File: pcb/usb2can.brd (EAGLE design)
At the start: 57.8 x 17.2 mm, 35 parts, among them CON1 USB_A_MALESMD, IC1 ADM3053M, IC2 LD117AS33TR, K2 61900419521

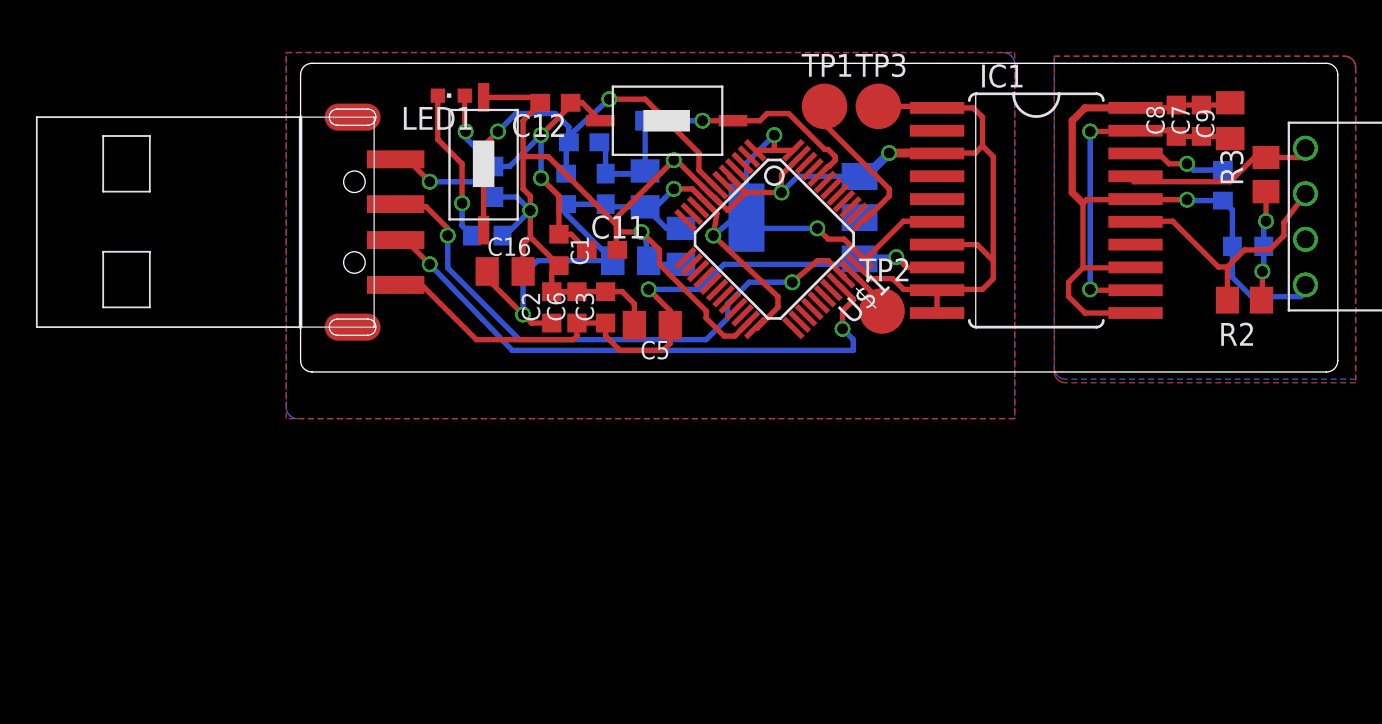
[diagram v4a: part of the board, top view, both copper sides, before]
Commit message: pcb: fix capacitor values for ADM3053
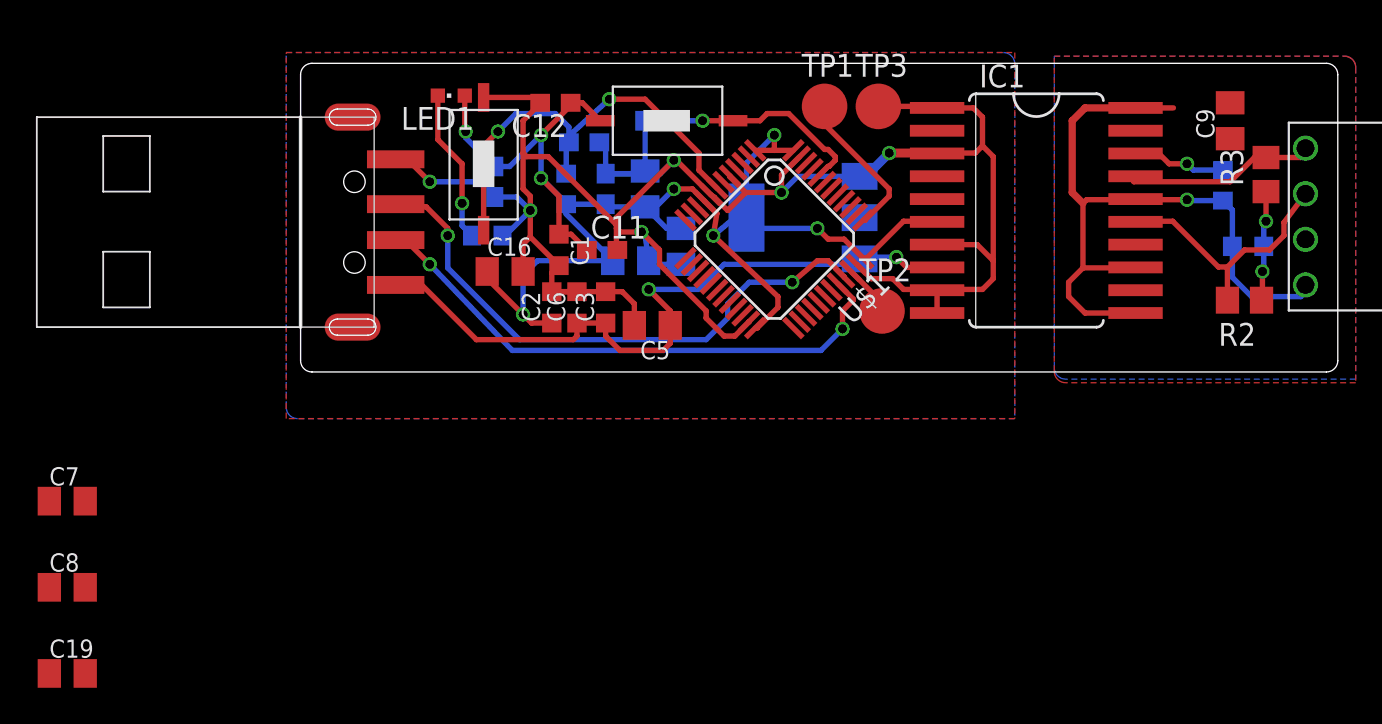
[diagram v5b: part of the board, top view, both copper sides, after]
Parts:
- added C19: 100n, rcl:C0805K
- C7: value 100n -> 10n; device rcl:C0603K -> rcl:C0805K
- C8: value 10n -> 10u; device rcl:C0603K -> rcl:C0805K
- C9: value 10u -> 100n
- moved C8 67.0 mm to (89.8, -15.0), turned to 0 degrees
- moved C7 66.7 mm to (89.8, -10.2), turned to 0 degrees
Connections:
- removed net VISO: C7.1, C8.1, C9.1, IC1.12, IC1.19
- new net N$10: C7.1, C9.1, IC1.19
- new net N$8: C19.1, C8.1, IC1.12
- net GNDA: now also C19.2
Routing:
- net VISO: track 19.4 -> 0.00 mm, vias 2 -> 0
- net GNDA: track 44.1 -> 40.8 mm
- net USB_DM: track 32.7 -> 31.1 mm

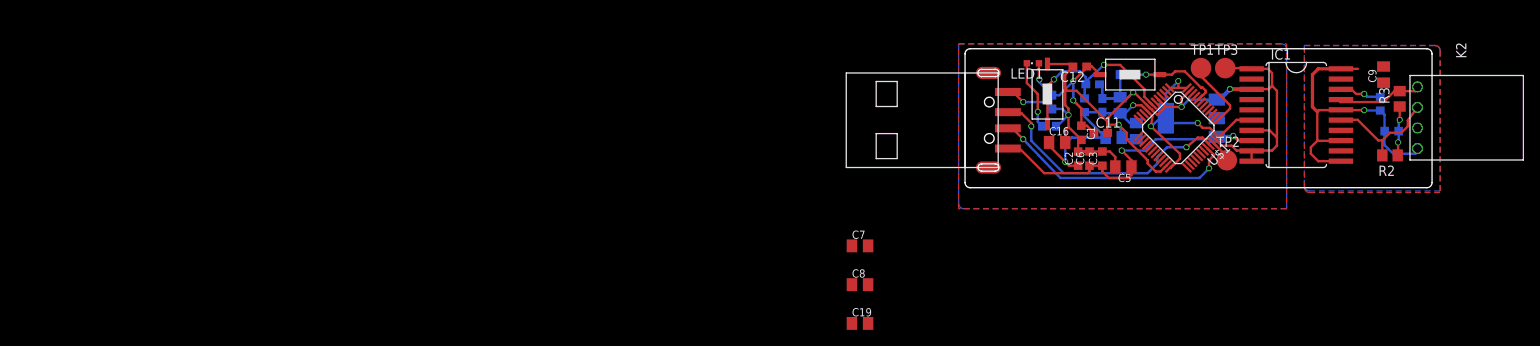
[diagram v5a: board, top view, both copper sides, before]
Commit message: pcb: final routing and small schamtic fixes
 * Testpad for UART TX
 * 4 User LEDs
 * 1 User Button
 * RCA CAN-connector
 * Bypass capacitor for BOOT0
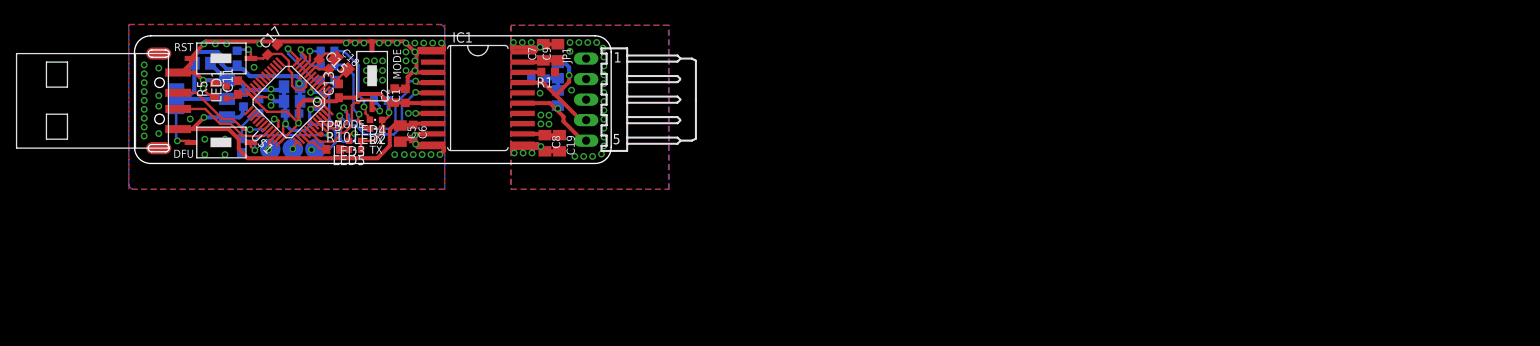
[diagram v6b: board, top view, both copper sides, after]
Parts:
- removed K2: 61900419521, Wuerth_Elektronik_eiCan_Wire_to_Board_Connectors:61900419521
- added C20: 100n, rcl:C0603
- added GND: TPB2,54, testpad:B2,54
- added JP1: SABH, rca_stecker:7395-05
- added LED2, LED3, LED4, LED5: GREEN, led:CHIPLED_0603
- added R10, R7, R8, R9: 330R, resistor:R0603
- added R11: 10k, resistor:R0603
- added S3: MICRO_SWITCH_3X6X2.5S, micro_switch:MICRO_SWITCH_3X6X2.5
- added U$2: (no value), rca_templates:LOGO_SILK_BOT
- IC2: value LD117AS33TR -> LD1117S33
- TP3: value TPB2,54 -> TPSTP07R; device testpad:B2,54 -> testpad:TP07R
- moved IC2 122.5 mm to (8.30, 8.00)
- moved TP2 118.4 mm to (16.8, 1.80), flipped to the bottom
- moved C4 113.2 mm to (8.40, 12.4)
- moved TP1 112.8 mm to (19.6, 1.80), flipped to the bottom
- moved S1 112.8 mm to (10.7, 2.60)
- moved TP3 112.2 mm to (23.1, 3.62)
- moved U$1 110.1 mm to (19.1, 7.60), turned to 135 degrees
- moved R4 107.5 mm to (15.4, 7.10), turned to 270 degrees
- moved C11 106.9 mm to (12.8, 9.40), turned to 90 degrees
- moved C3 106.6 mm to (13.5, 7.90), flipped to the bottom
- moved C10 105.8 mm to (50.0, 10.5)
- moved R6 105.1 mm to (12.7, 13.1)
- moved C14 104.6 mm to (19.5, 7.70), turned to 0 degrees
- moved R3 104.3 mm to (52.4, 11.5), flipped to the bottom
- moved R5 103.4 mm to (9.90, 9.10), flipped to the top, turned to 90 degrees
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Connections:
- removed net CAN_RX: U$1.45
- removed net CAN_TX: U$1.46
- new net N$11: R11.2, S3.2, U$1.41
- new net N$12: LED3.C, R8.2
- new net N$13: LED4.C, R9.2
- new net N$14: R9.1, U$1.10
- new net N$15: R7.1, U$1.11
- new net N$16: R8.1, U$1.12
- new net N$17: LED5.C, R10.2
- new net N$18: R10.1, U$1.39
- new net N$9: LED2.C, R7.2
- new net TX: TP3.TP, U$1.42
- net +3V3: now also LED2.A, LED3.A, LED4.A, LED5.A, R11.1
- net CAN_RXD: now also U$1.45
- net CAN_TXD: now also U$1.46
- net GND: now also C20.2, GND.TP, S3.1; no longer TP3.TP
- net GNDA: now also JP1.3; no longer K2.4
- net N$2: now also JP1.5; no longer K2.2
- net N$3: now also JP1.4; no longer K2.1
- net N$6: now also C20.1
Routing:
- net CAN_RXD: track 0.00 -> 23.3 mm, vias 0 -> 2
- net GNDA: track 40.8 -> 18.3 mm, vias 1 -> 35
- net CAN_TXD: track 0.00 -> 19.4 mm, vias 0 -> 2
- net USB_DM: track 31.1 -> 12.9 mm, vias 2 -> 0
- net +3V3: track 82.5 -> 100.3 mm, vias 8 -> 5
- net N$11: track 0.00 -> 15.6 mm, vias 0 -> 1
- net USB_DP: track 32.1 -> 16.8 mm
- net N$12: track 0.00 -> 12.4 mm, vias 0 -> 1
- net N$13: track 0.00 -> 11.4 mm, vias 0 -> 1
- net N$9: track 0.00 -> 10.8 mm, vias 0 -> 1
- net N$7: track 24.8 -> 14.9 mm, vias 2 -> 1
- net N$6: track 11.6 -> 20.5 mm, vias 1 -> 2
- net N$16: track 0.00 -> 8.15 mm, vias 0 -> 1
- net SWDCLK: track 8.66 -> 1.33 mm, vias 0 -> 1
- net N$5: track 8.59 -> 1.67 mm, vias 1 -> 0
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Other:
- board size 57.8 x 17.2 mm -> 59 x 15.8 mm
- board text added: "2016"
- board text added: "CLK"
- board text added: "DFU"
- board text added: "GND"
- board text added: "HW: Daniel SW: Kevin"
- board text added: "IO"
- board text added: "MODE"
- board text added: "RST"
- board text added: "RX"
- board text added: "Rev. 1"
- board text added: "SWD"
- board text added: "TX"

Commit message: final order of rev1
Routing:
- net GNDA: vias 35 -> 30
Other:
- board text added: "CANH"
- board text added: "CANL"
- board text added: "xpcc.io"
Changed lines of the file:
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@@
 <layer number="14" name="Route14" color="1" fill="6" visible="no" active="no"/>
 <layer number="15" name="Route15" color="4" fill="6" visible="no" active="no"/>
-<layer number="16" name="Bottom" color="1" fill="1" visible="yes" active="yes"/>
+<layer number="16" name="Bottom" color="1" fill="1" visible="no" active="yes"/>
 <layer number="17" name="Pads" color="2" fill="1" visible="yes" active="yes"/>
 <layer number="18" name="Vias" color="2" fill="1" visible="yes" active="yes"/>
 <layer number="19" name="Unrouted" color="6" fill="1" visible="yes" active="yes"/>
 <layer number="20" name="Dimension" color="15" fill="1" visible="yes" active="yes"/>
-<layer number="21" name="tPlace" color="7" fill="1" visible="yes" active="yes"/>
-<layer number="22" name="bPlace" color="7" fill="1" visible="yes" active="yes"/>
+<layer number="21" name="tPlace" color="7" fill="1" visible="no" active="yes"/>
+<layer number="22" name="bPlace" color="7" fill="1" visible="no" active="yes"/>
 <layer number="23" name="tOrigins" color="15" fill="1" visible="yes" active="yes"/>
-<layer number="24" name="bOrigins" color="15" fill="1" visible="yes" active="yes"/>
+<layer number="24" name="bOrigins" color="15" fill="1" visible="no" active="yes"/>
 <layer number="25" name="tNames" color="7" fill="1" visible="no" active="yes"/>
 <layer number="26" name="bNames" color="7" fill="1" visible="no" active="yes"/>
@@
 <layer number="38" name="bTest" color="7" fill="1" visible="no" active="yes"/>
 <layer number="39" name="tKeepout" color="4" fill="11" visible="yes" active="yes"/>
-<layer number="40" name="bKeepout" color="1" fill="11" visible="yes" active="yes"/>
+<layer number="40" name="bKeepout" color="1" fill="11" visible="no" active="yes"/>
 <layer number="41" name="tRestrict" color="4" fill="10" visible="yes" active="yes"/>
-<layer number="42" name="bRestrict" color="1" fill="10" visible="yes" active="yes"/>
+<layer number="42" name="bRestrict" color="1" fill="10" visible="no" active="yes"/>
 <layer number="43" name="vRestrict" color="2" fill="10" visible="yes" active="yes"/>
 <layer number="44" name="Drills" color="7" fill="1" visible="no" active="yes"/>
@@
 <layer number="50" name="dxf" color="7" fill="1" visible="no" active="no"/>
 <layer number="51" name="tDocu" color="7" fill="1" visible="yes" active="yes"/>
-<layer number="52" name="bDocu" color="7" fill="1" visible="yes" active="yes"/>
+<layer number="52" name="bDocu" color="7" fill="1" visible="no" active="yes"/>
 <layer number="53" name="tGND_GNDA" color="7" fill="9" visible="no" active="no"/>
 <layer number="54" name="bGND_GNDA" color="1" fill="9" visible="no" active="no"/>
@@
 SW: Kevin</text>
 <text x="44.9" y="1.2" size="1" layer="60" ratio="16" rot="MR0">Rev. 1</text>
+<text x="44.1" y="2.9" size="0.6" layer="60" ratio="16" rot="MR0">xpcc.io</text>
+<text x="50.7" y="4.9" size="1" layer="59" ratio="16">CANH</text>
+<text x="54.1" y="0.7" size="1" layer="59" ratio="16">CANL</text>
+<text x="51.6" y="7.4" size="1" layer="59" ratio="16">GND</text>
 </plain>
 <attributes>
@@
 <vertex x="66.2" y="17.1"/>
 </polygon>
-<via x="50.3" y="4.9" extent="1-16" drill="0.5"/>
+<wire x1="50.3" y1="4.9" x2="50.3" y2="4.9" width="0" layer="19" extent="1-16"/>
 <via x="50.2" y="8.7" extent="1-16" drill="0.5"/>
 <via x="50.3" y="2.1" extent="1-16" drill="0.5"/>
@@
 <via x="48.1" y="1.3" extent="1-16" drill="0.5"/>
 <via x="49.2" y="1.3" extent="1-16" drill="0.5"/>
-<via x="50.3" y="6" extent="1-16" drill="0.5"/>
+<via x="50.3" y="4.9" extent="1-16" drill="0.5"/>
 <contactref element="JP1" pad="3"/>
 <via x="53.9" y="14.97" extent="1-16" drill="0.5"/>
@@
 <via x="58.1" y="3.27" extent="1-16" drill="0.5"/>
 <via x="58.1" y="2.17" extent="1-16" drill="0.5"/>
-<via x="57.8" y="1.17" extent="1-16" drill="0.5"/>
-<via x="56.7" y="0.87" extent="1-16" drill="0.5"/>
-<via x="55.6" y="0.87" extent="1-16" drill="0.5"/>
-<via x="54.5" y="0.87" extent="1-16" drill="0.5"/>
+<wire x1="57.8" y1="1.17" x2="57.8" y2="1.17" width="0" layer="19" extent="1-16"/>
+<wire x1="56.7" y1="0.87" x2="56.7" y2="0.87" width="0" layer="19" extent="1-16"/>
+<wire x1="55.6" y1="0.87" x2="55.6" y2="0.87" width="0" layer="19" extent="1-16"/>
+<wire x1="54.5" y1="0.87" x2="54.5" y2="0.87" width="0" layer="19" extent="1-16"/>
 <via x="54.1" y="9.07" extent="1-16" drill="0.5"/>
-<via x="51.3" y="4.87" extent="1-16" drill="0.5"/>
-<via x="51.3" y="5.97" extent="1-16" drill="0.5"/>
+<wire x1="51.3" y1="4.87" x2="51.3" y2="4.87" width="0" layer="19" extent="1-16"/>
+<via x="50.3" y="5.97" extent="1-16" drill="0.5"/>
 <via x="53.9" y="13.87" extent="1-16" drill="0.5"/>
 <wire x1="49.2" y1="1.3" x2="49.3" y2="1.4" width="0.5" layer="1"/>
@@
 <wire x1="46.7" y1="2" x2="46.8" y2="1.9" width="0.5" layer="1"/>
 <wire x1="46.8" y1="1.9" x2="49.9" y2="1.9" width="0.5" layer="1"/>
+<via x="51.1" y="6.57" extent="1-16" drill="0.5"/>
 </signal>
 <signal name="N$1">

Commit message: pcb: update schematic with correct values
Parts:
- C10: value 47p -> 47n
- LED2: value GREEN -> BLUE
- LED3: value GREEN -> RED
- LED4: value GREEN -> WHITE
- R1: value (none) -> 8.2k
- R2, R3: value 60R -> 56R
- R7, R9: value 330R -> 33R
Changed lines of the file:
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@@
 <layer number="14" name="Route14" color="1" fill="6" visible="no" active="no"/>
 <layer number="15" name="Route15" color="4" fill="6" visible="no" active="no"/>
-<layer number="16" name="Bottom" color="1" fill="1" visible="no" active="yes"/>
+<layer number="16" name="Bottom" color="1" fill="1" visible="yes" active="yes"/>
 <layer number="17" name="Pads" color="2" fill="1" visible="yes" active="yes"/>
 <layer number="18" name="Vias" color="2" fill="1" visible="yes" active="yes"/>
 <layer number="19" name="Unrouted" color="6" fill="1" visible="yes" active="yes"/>
 <layer number="20" name="Dimension" color="15" fill="1" visible="yes" active="yes"/>
-<layer number="21" name="tPlace" color="7" fill="1" visible="no" active="yes"/>
-<layer number="22" name="bPlace" color="7" fill="1" visible="no" active="yes"/>
+<layer number="21" name="tPlace" color="7" fill="1" visible="yes" active="yes"/>
+<layer number="22" name="bPlace" color="7" fill="1" visible="yes" active="yes"/>
 <layer number="23" name="tOrigins" color="15" fill="1" visible="yes" active="yes"/>
-<layer number="24" name="bOrigins" color="15" fill="1" visible="no" active="yes"/>
+<layer number="24" name="bOrigins" color="15" fill="1" visible="yes" active="yes"/>
 <layer number="25" name="tNames" color="7" fill="1" visible="no" active="yes"/>
 <layer number="26" name="bNames" color="7" fill="1" visible="no" active="yes"/>
@@
 <layer number="38" name="bTest" color="7" fill="1" visible="no" active="yes"/>
 <layer number="39" name="tKeepout" color="4" fill="11" visible="yes" active="yes"/>
-<layer number="40" name="bKeepout" color="1" fill="11" visible="no" active="yes"/>
+<layer number="40" name="bKeepout" color="1" fill="11" visible="yes" active="yes"/>
 <layer number="41" name="tRestrict" color="4" fill="10" visible="yes" active="yes"/>
-<layer number="42" name="bRestrict" color="1" fill="10" visible="no" active="yes"/>
+<layer number="42" name="bRestrict" color="1" fill="10" visible="yes" active="yes"/>
 <layer number="43" name="vRestrict" color="2" fill="10" visible="yes" active="yes"/>
 <layer number="44" name="Drills" color="7" fill="1" visible="no" active="yes"/>
@@
 <layer number="50" name="dxf" color="7" fill="1" visible="no" active="no"/>
 <layer number="51" name="tDocu" color="7" fill="1" visible="yes" active="yes"/>
-<layer number="52" name="bDocu" color="7" fill="1" visible="no" active="yes"/>
+<layer number="52" name="bDocu" color="7" fill="1" visible="yes" active="yes"/>
 <layer number="53" name="tGND_GNDA" color="7" fill="9" visible="no" active="no"/>
 <layer number="54" name="bGND_GNDA" color="1" fill="9" visible="no" active="no"/>
@@
 <element name="C5" library="rcl" package="C0805K" value="10u" x="32.9" y="3.7" rot="R270"/>
 <element name="C6" library="rcl" package="C0603K" value="100n" x="34.5" y="3.9" rot="R270"/>
-<element name="R1" library="rcl" package="R0603" value="" x="51.2" y="11.3" rot="R180"/>
+<element name="R1" library="rcl" package="R0603" value="8.2k" x="51.2" y="11.3" rot="R180"/>
 <element name="C9" library="rcl" package="C0805K" value="100n" x="52.4" y="13.76" rot="R90"/>
 <element name="U$1" library="stm32" package="TQFP48" value="STM32F072CT" x="19.1" y="7.6" rot="R135"/>
-<element name="R2" library="rcl" package="R0805" value="60R" x="52.4" y="8.1" rot="MR270"/>
-<element name="R3" library="rcl" package="R0805" value="60R" x="52.4" y="11.5" rot="MR90"/>
-<element name="C10" library="rcl" package="C0603K" value="47p" x="50" y="10.5" rot="MR0"/>
+<element name="R2" library="rcl" package="R0805" value="56R" x="52.4" y="8.1" rot="MR270"/>
+<element name="R3" library="rcl" package="R0805" value="56R" x="52.4" y="11.5" rot="MR90"/>
+<element name="C10" library="rcl" package="C0603K" value="47n" x="50" y="10.5" rot="MR0"/>
 <element name="C11" library="rcl" package="C0603" value="100n" x="12.8" y="9.4" rot="R90"/>
 <element name="C12" library="rcl" package="C0603" value="100n" x="19.5" y="6.18284375" rot="MR0"/>
@@
 <element name="C8" library="rcl" package="C0805K" value="10u" x="50.8" y="2.5" rot="R270"/>
 <element name="C19" library="rcl" package="C0805K" value="100n" x="52.6" y="2.5" rot="R270"/>
-<element name="LED2" library="led" package="CHIPLED_0603" value="GREEN" x="29.9" y="4.3" rot="R90"/>
-<element name="R7" library="resistor" package="R0603" value="330R" x="23.9" y="12.1" rot="MR180"/>
+<element name="LED2" library="led" package="CHIPLED_0603" value="BLUE" x="29.9" y="4.3" rot="R90"/>
+<element name="R7" library="resistor" package="R0603" value="33R" x="23.9" y="12.1" rot="MR180"/>
 <element name="S3" library="micro_switch" package="MICRO_SWITCH_3X6X2.5" value="MICRO_SWITCH_3X6X2.5S" x="29.4" y="10.858575" rot="R270"/>
-<element name="LED3" library="led" package="CHIPLED_0603" value="GREEN" x="27.3" y="2.8" rot="R90"/>
+<element name="LED3" library="led" package="CHIPLED_0603" value="RED" x="27.3" y="2.8" rot="R90"/>
 <element name="R8" library="resistor" package="R0603" value="330R" x="23.9" y="10.3" rot="MR180"/>
-<element name="LED4" library="led" package="CHIPLED_0603" value="GREEN" x="29.9" y="5.4" rot="R90"/>
-<element name="R9" library="resistor" package="R0603" value="330R" x="23.9" y="13.9" rot="MR180"/>
+<element name="LED4" library="led" package="CHIPLED_0603" value="WHITE" x="29.9" y="5.4" rot="R90"/>
+<element name="R9" library="resistor" package="R0603" value="33R" x="23.9" y="13.9" rot="MR180"/>
 <element name="LED5" library="led" package="CHIPLED_0603" value="GREEN" x="27.3" y="1.7" rot="R90"/>
 <element name="R10" library="resistor" package="R0603" value="330R" x="24.6" y="1.75"/>
@@
 <vertex x="66.2" y="17.1"/>
 </polygon>
-<wire x1="50.3" y1="4.9" x2="50.3" y2="4.9" width="0" layer="19" extent="1-16"/>
 <via x="50.2" y="8.7" extent="1-16" drill="0.5"/>
 <via x="50.3" y="2.1" extent="1-16" drill="0.5"/>
@@
 <via x="58.1" y="3.27" extent="1-16" drill="0.5"/>
 <via x="58.1" y="2.17" extent="1-16" drill="0.5"/>
-<wire x1="57.8" y1="1.17" x2="57.8" y2="1.17" width="0" layer="19" extent="1-16"/>
-<wire x1="56.7" y1="0.87" x2="56.7" y2="0.87" width="0" layer="19" extent="1-16"/>
-<wire x1="55.6" y1="0.87" x2="55.6" y2="0.87" width="0" layer="19" extent="1-16"/>
-<wire x1="54.5" y1="0.87" x2="54.5" y2="0.87" width="0" layer="19" extent="1-16"/>
 <via x="54.1" y="9.07" extent="1-16" drill="0.5"/>
-<wire x1="51.3" y1="4.87" x2="51.3" y2="4.87" width="0" layer="19" extent="1-16"/>
 <via x="50.3" y="5.97" extent="1-16" drill="0.5"/>
 <via x="53.9" y="13.87" extent="1-16" drill="0.5"/>
